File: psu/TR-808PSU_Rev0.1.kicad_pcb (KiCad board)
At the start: 2 copper layers, 142.9 x 119.4 mm, 67 parts, among them IC1 uA7805, IC2 TA7179P, P1 1, P10 10, P11 11, P12 12, P13 13, P14 14, P15 15, P16 16, P17 17, P18 18, P19 19, P2 2, P20 20, P21 21, P22 22, P3 3, P4 4, P5 5, P6 6, P7 7, P8 8, P9 9, Q1 2SB596, Q2 2SD880

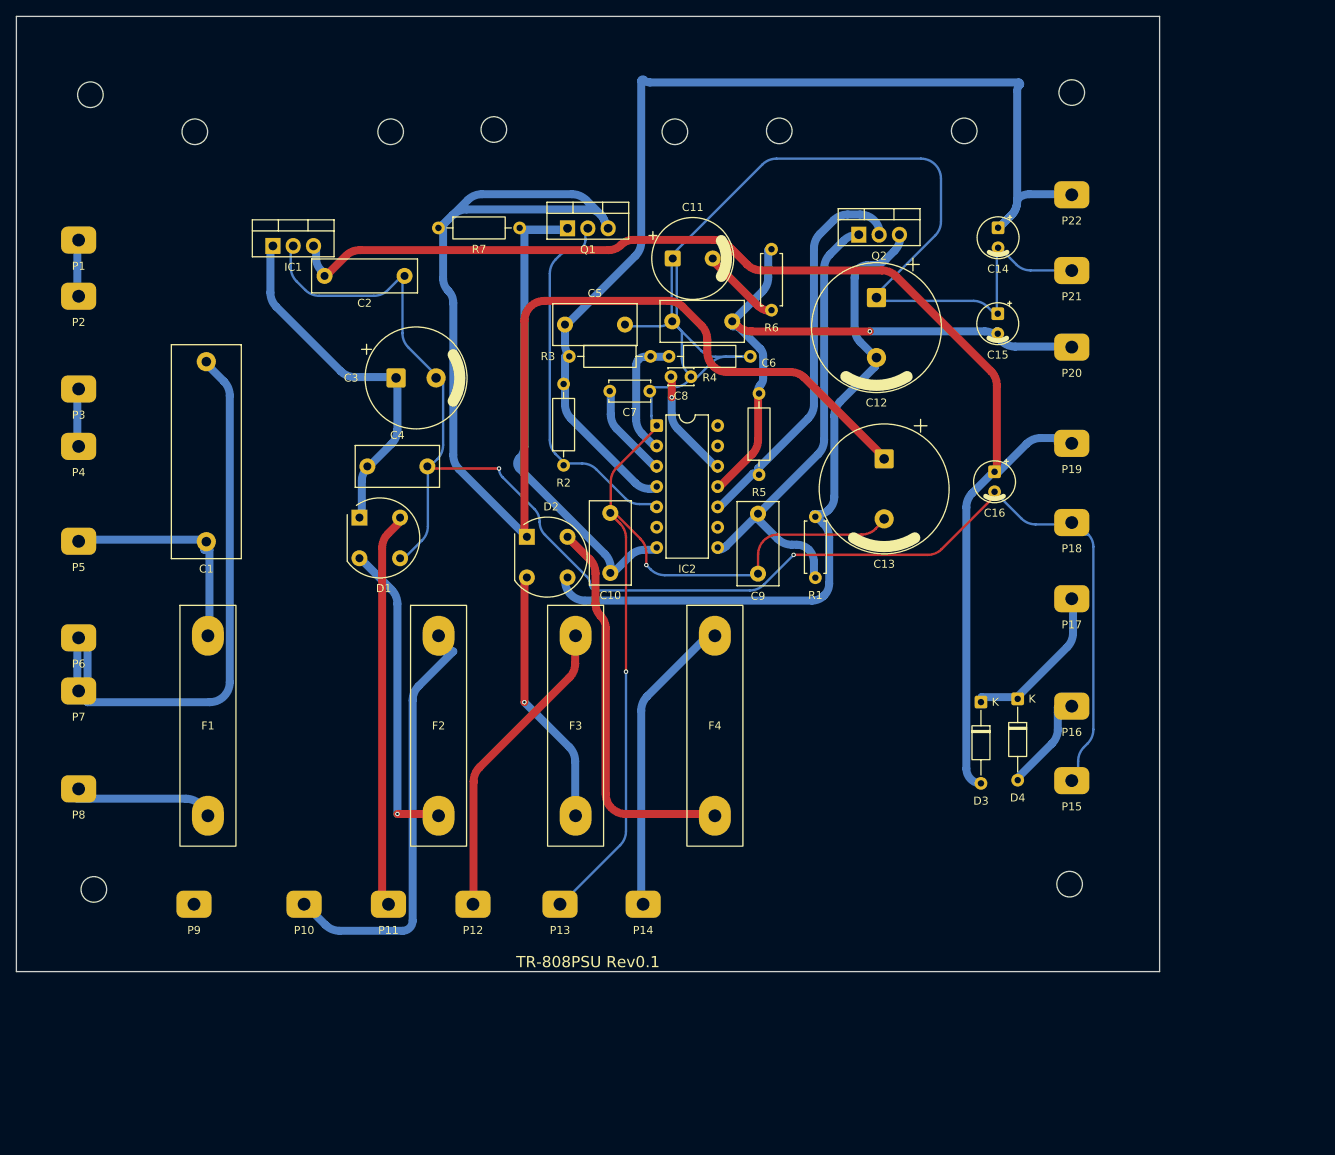
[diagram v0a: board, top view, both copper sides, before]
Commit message: Alle Bahnen 1,0 mm, Pad-Haarnadeln entfernt, Beschriftung frei von Bahnen
verbreitern.py (schmale Netze auf 1,0 mm, DRC-geprueft), padstummel.py (Knicke im Pad),
silk.py meidet Bahnen. DRC 0 Fehler, 0 offen, Netzabstand 6,5 mm.

Co-Authored-By: Claude Sonnet 5.5 <noreply@anthropic.com>
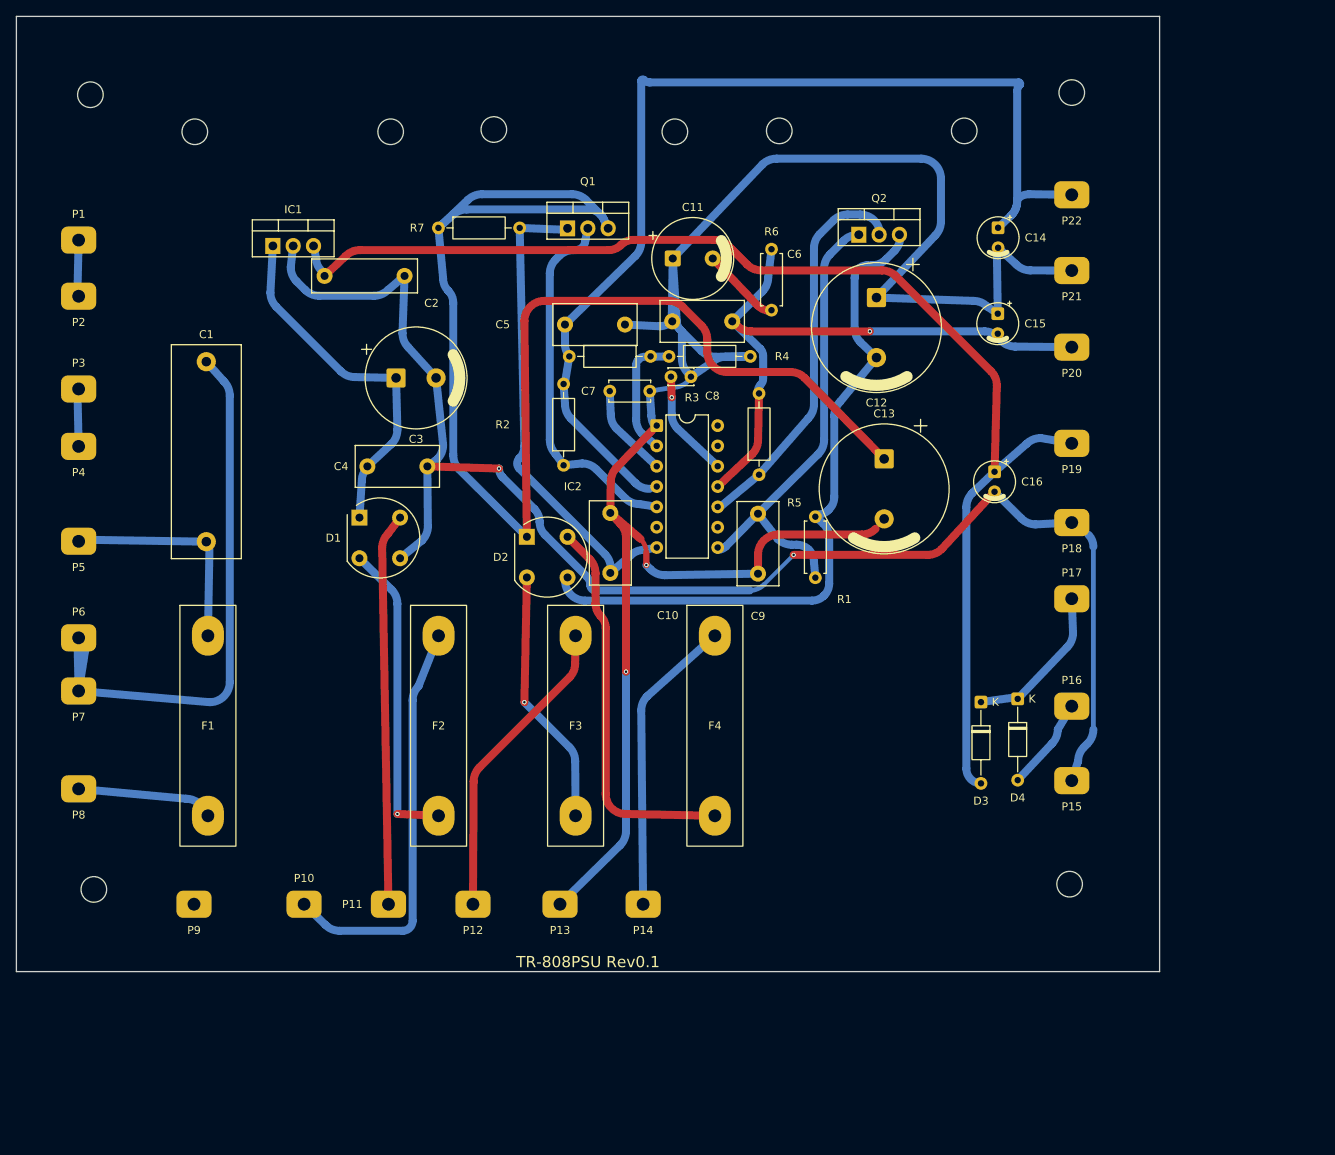
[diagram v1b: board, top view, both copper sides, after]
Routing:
- net /GND15: track 269.0 -> 256.8 mm
- net /GND5: track 193.3 -> 185.4 mm
- net /VB1: track 67.6 -> 59.9 mm
- net /+15V: track 142.3 -> 135.4 mm
- net /-15V: track 82.9 -> 76.7 mm
- net /+5V: track 165.8 -> 159.8 mm
- net /RAW15N: track 89.9 -> 86.3 mm
- net /PRI_8: track 18.9 -> 15.4 mm
- net /AC5_RAW: track 55.0 -> 51.8 mm
- net /SW_A: track 29.7 -> 26.9 mm
- net /SW_B: track 77.8 -> 75.2 mm
- net /RAW5: track 47.6 -> 45.1 mm
- net /RAW15P: track 174.9 -> 173.1 mm
- net /BAT_P: track 13.2 -> 11.6 mm
- net /ADJ: track 16.5 -> 15.0 mm
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
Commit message: Mehr Abstand: Regel 0,25 mm, Bahnen neu, Nachbessern der Breite
Abstandsregel von 0,2 auf 0,25 mm (Router, Glaetten, DRC); verbreitern.py bessert Reststellen nach,
padstummel.py bindet Boegen in der Padrandzone an, silk.py weicht Bahnen aus.

Co-Authored-By: Claude Sonnet 5.5 <noreply@anthropic.com>
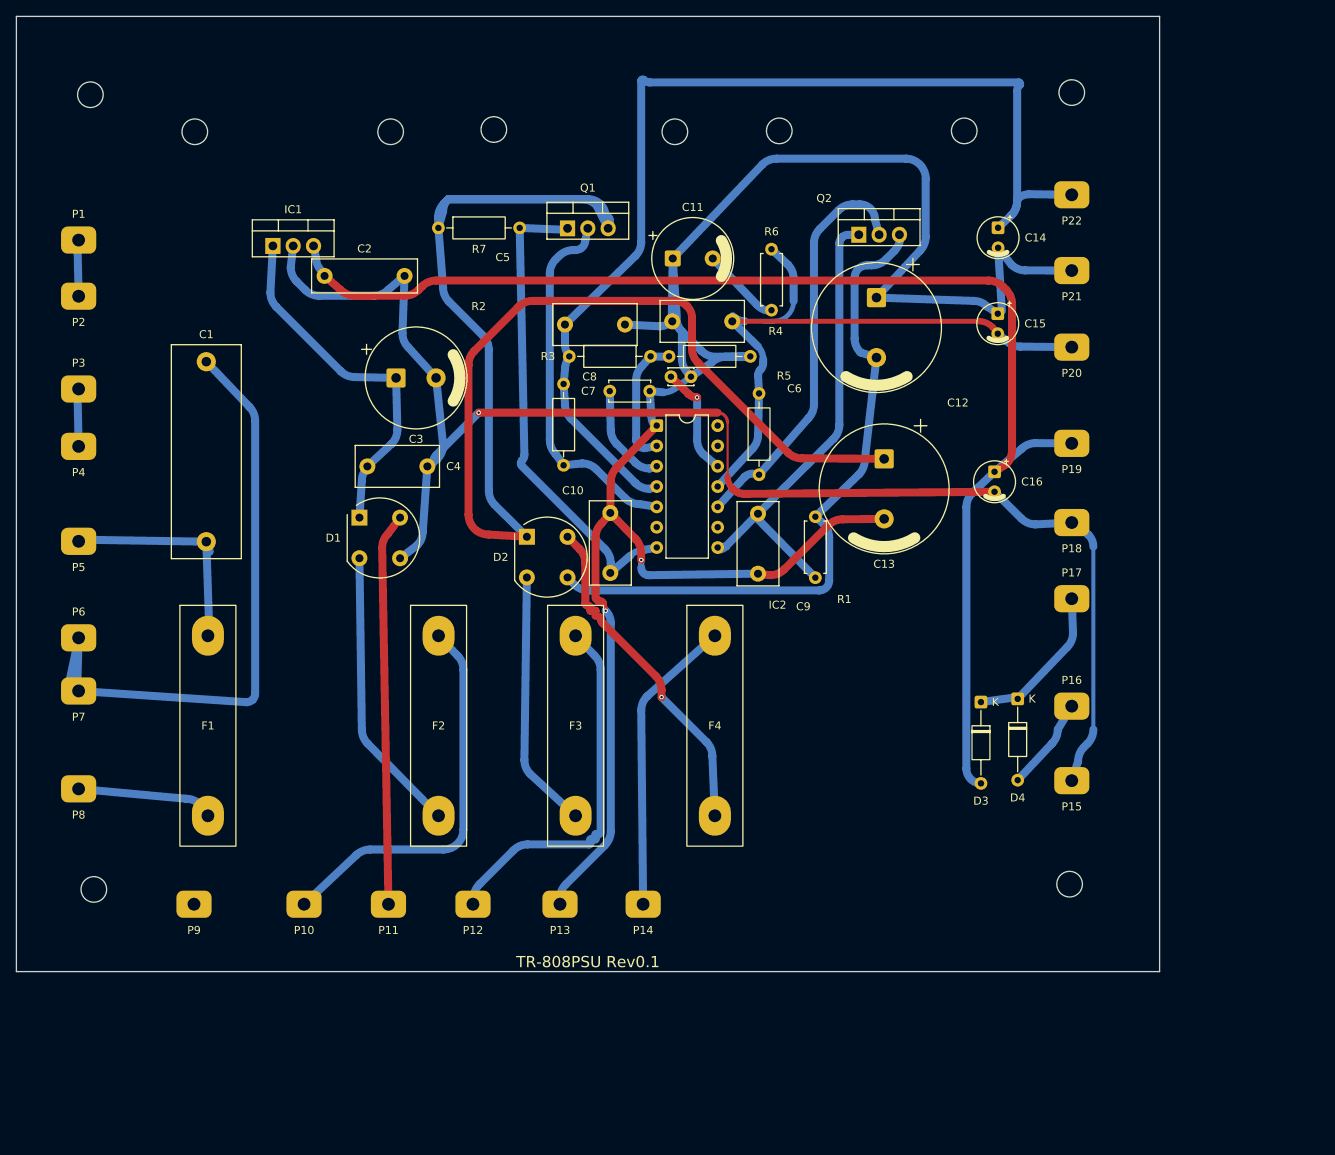
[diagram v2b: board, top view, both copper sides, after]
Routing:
- net /RAW15P: track 173.1 -> 191.3 mm
- net /-15V: track 76.7 -> 84.4 mm, vias 1 -> 0
- net /AC15_RAW_A: track 38.6 -> 46.0 mm
- net /+5V: track 159.8 -> 166.3 mm
- net /AC15_B: track 48.8 -> 42.8 mm, vias 0 -> 1
- net /SW_A: track 26.9 -> 30.9 mm
- net /SW_B: track 75.2 -> 79.0 mm
- net Net-(D1-Pad2): track 39.0 -> 36.0 mm, vias 1 -> 0
- net /AC5_RAW: track 51.8 -> 49.2 mm
- net /GND15: track 256.8 -> 254.4 mm
- net /COL2: track 49.2 -> 50.6 mm
- net /RAW15N: track 86.3 -> 85.0 mm
- net /COMP1: track 11.7 -> 13.0 mm
- net /+15V: track 135.4 -> 136.6 mm
- net /ADJ: track 15.0 -> 16.2 mm
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
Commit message: Zickzack-Stuecke in den Bahnen gerade gezogen (zickzack.py)
Folgen aus kurzen Teilen werden durch ein Segment ersetzt, wenn die DRC danach keinen
neuen Fehler zeigt (9 von 10 Stellen). Beispiel: Treppe unter F3.

Co-Authored-By: Claude Sonnet 5.5 <noreply@anthropic.com>
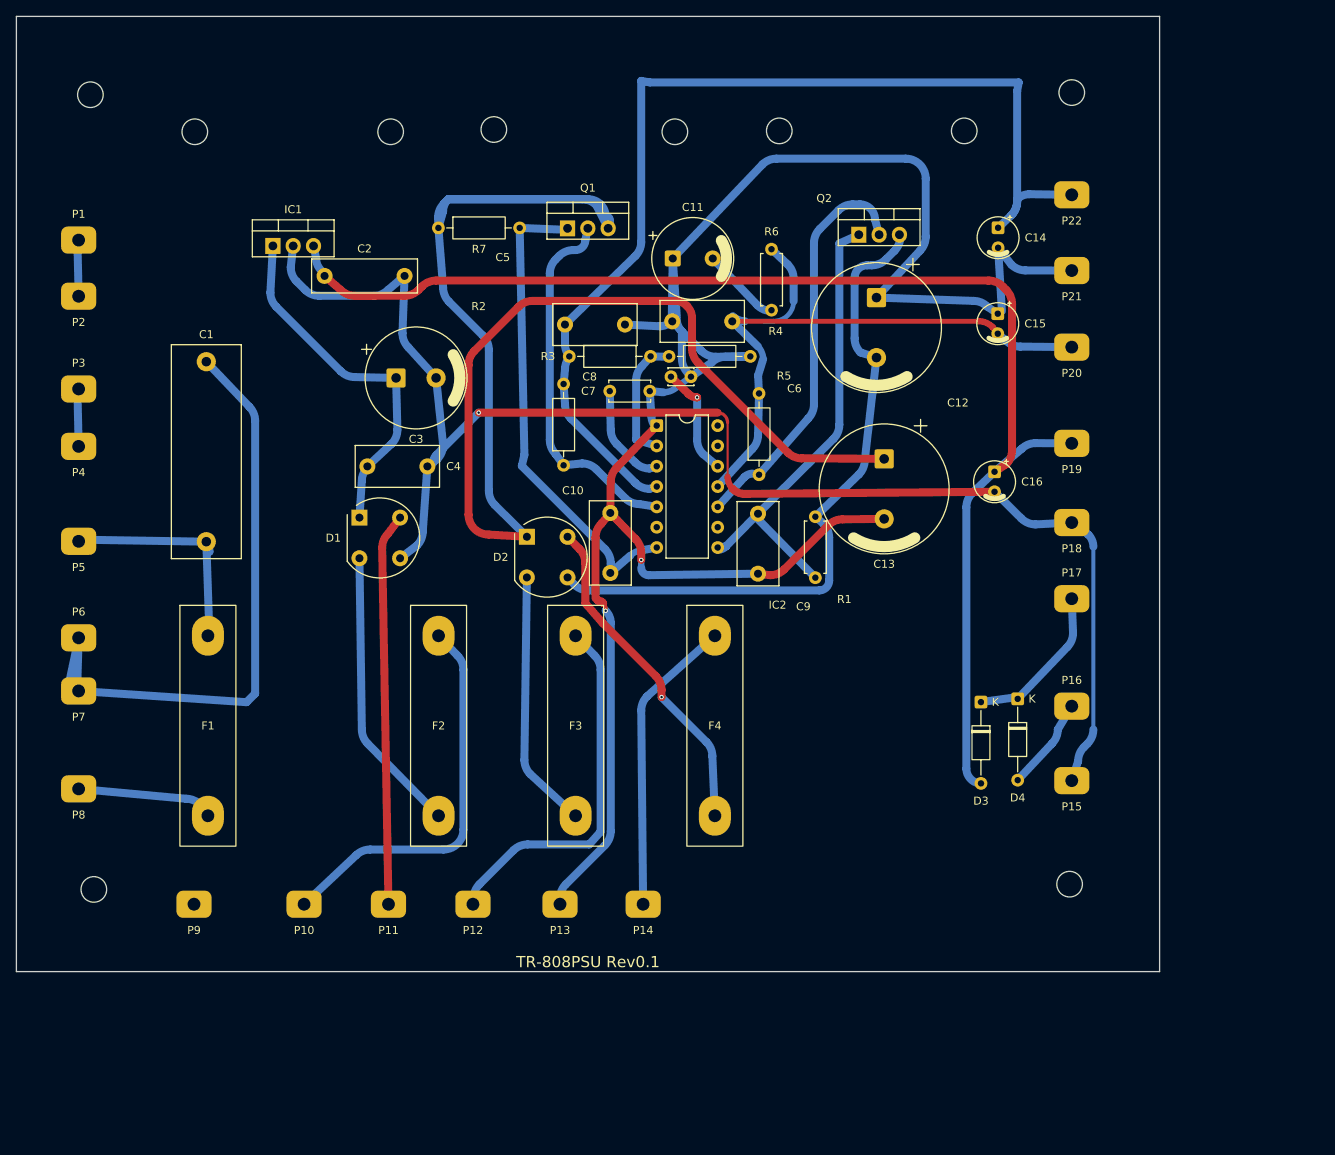
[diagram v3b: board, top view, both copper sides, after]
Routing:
- net /AC15_B: track 42.8 -> 41.9 mm
- net /AC15_RAW_A: track 46.0 -> 45.4 mm
- net /ADJ: track 16.2 -> 15.7 mm

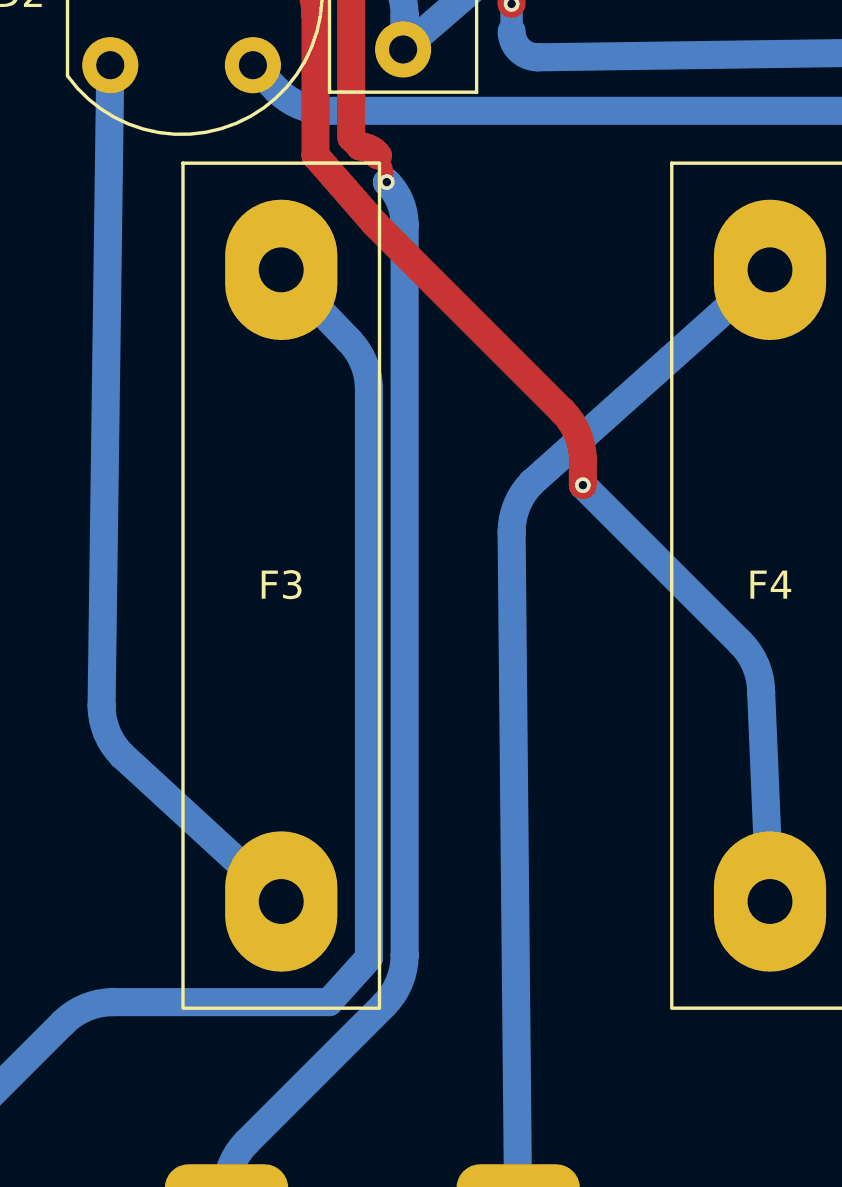
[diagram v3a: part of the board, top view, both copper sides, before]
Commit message: GND15 neben F3 verlegt: 2,2 mm Abstand statt 0,27 mm
korrekturen.py (DRC-geprueft, in make.py eingehaengt).

Co-Authored-By: Claude Sonnet 5.5 <noreply@anthropic.com>
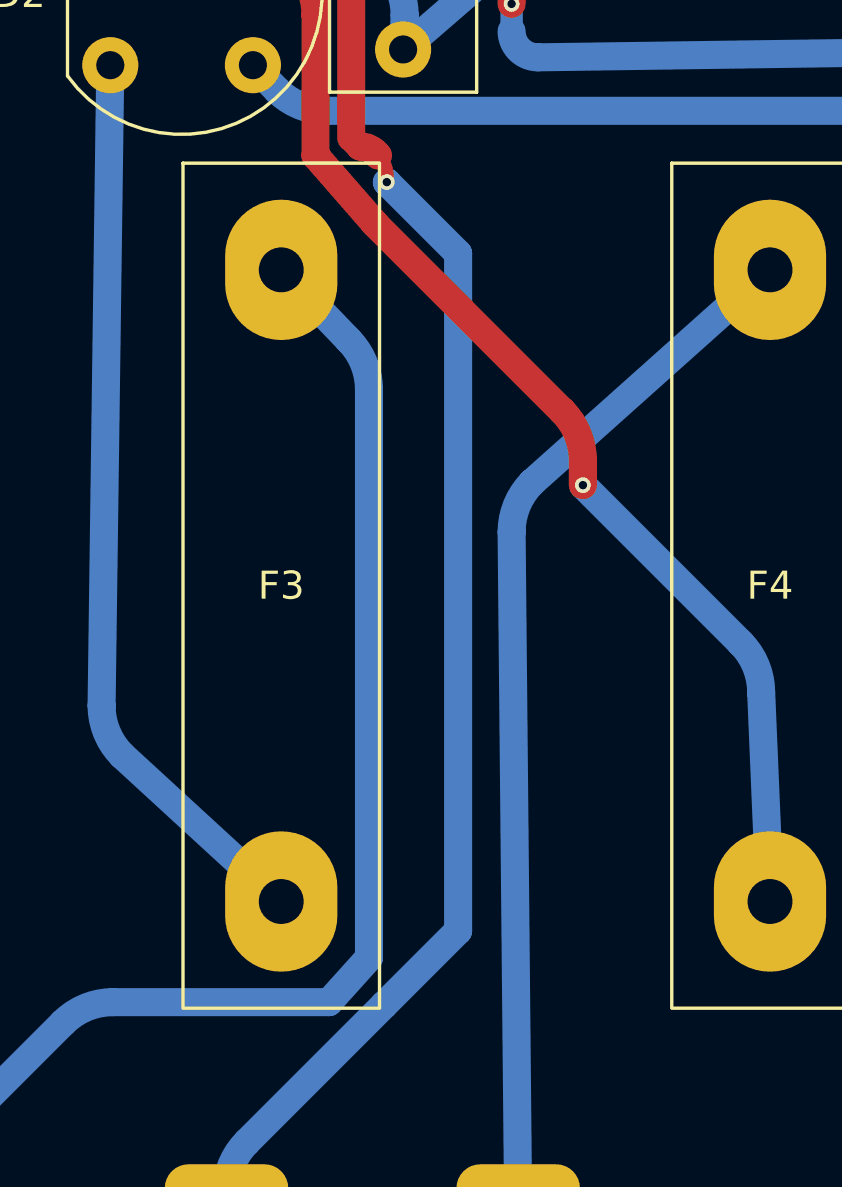
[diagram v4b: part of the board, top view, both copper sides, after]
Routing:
- net /GND15: track 254.4 -> 256.2 mm
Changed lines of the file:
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@@
-	)
-	(segment
-		(start 74.295 75.8101)
-		(end 74.295 101.8345)
-		(width 1)
-		(layer "B.Cu")
-		(net "/GND15")
 	)
 	(segment
@@
 		(mid 78.3784 69.5766)
 		(end 79.0385 69.85)
-		(width 1)
-		(layer "B.Cu")
-		(net "/GND15")
-	)
-	(arc
-		(start 73.6727 74.3077)
-		(mid 74.1333 74.997)
-		(end 74.295 75.8101)
 		(width 1)
 		(layer "B.Cu")
@@
 		(mid 94.0588 17.9703)
 		(end 93.2478 18.5122)
-		(width 1)
-		(layer "B.Cu")
-		(net "/GND15")
-	)
-	(arc
-		(start 74.295 101.8345)
-		(mid 74.1047 102.7912)
-		(end 73.5628 103.6022)
 		(width 1)
 		(layer "B.Cu")
@@
 		(net "/AC15_B")
 	)
+	(segment
+		(start 73.6727 74.3077)
+		(end 76.2000 76.8350)
+		(width 1)
+		(layer "B.Cu")
+		(net "/GND15")
+	)
+	(segment
+		(start 76.2000 76.8350)
+		(end 76.2000 100.9650)
+		(width 1)
+		(layer "B.Cu")
+		(net "/GND15")
+	)
+	(segment
+		(start 76.2000 100.9650)
+		(end 73.5628 103.6022)
+		(width 1)
+		(layer "B.Cu")
+		(net "/GND15")
+	)
 )

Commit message: Handanpassung uebernommen, C8 und loses Bahnende korrigiert
Von Hand: Q2/R7/D3/C8 leicht verschoben, Bahnen teils neu. Korrigiert (korrekturen.py, DRC-geprueft):
C8-Abstaende, GND15-Ende bei (113/21), Polaritaetsbalken der kleinen Elkos nicht mehr auf dem Pad.
Fertigungsdaten, Ausdruck, Plots neu. DRC 0 Fehler, 0 offen.

Co-Authored-By: Claude Sonnet 5.5 <noreply@anthropic.com>
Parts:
- moved Q2 0.80 mm to (105.3, 26.5)
- moved D3 0.37 mm to (120.5, 85.3)
- moved C8 0.30 mm to (81.8, 45.3)
- moved R7 0.21 mm to (52.7, 26.6)
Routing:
- net /GND15: track 256.2 -> 240.5 mm
- net /SW_B: track 78.8 -> 68.7 mm
- net /+15V: track 136.3 -> 131.8 mm
- net /-15V: track 84.3 -> 87.3 mm
- net /GND5: track 185.6 -> 188.5 mm
- net /+5V: track 166.3 -> 168.1 mm
- net /COMP2: track 13.9 -> 15.2 mm
- net /COL2: track 50.6 -> 50.0 mm

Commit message: Kuehlkoerperbohrungen: 21,3 mm Abstand, mittig zu IC1, Q1, Q2
Je Regler ein Paar symmetrisch zum mittleren Anschluss (vorher 22,6 bis 24,5 mm, nicht mittig).
original_placement.py berechnet die Lage jetzt aus den Reglerpositionen. DRC 0 Fehler.

Co-Authored-By: Claude Sonnet 5.5 <noreply@anthropic.com>
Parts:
- moved H9 29.7 mm to (117.0, 34.6)
- moved H5 29.5 mm to (43.8, 34.6)
- moved H7 29.3 mm to (80.6, 34.6)
- moved C10 28.6 mm to (94.1, 90.2)
- moved C9 28.6 mm to (112.5, 90.3)
- moved H4 28.6 mm to (151.5, 129.1)
- moved C1 28.6 mm to (43.6, 86.3)
- moved C14 28.6 mm to (142.6, 47.1)
- moved C16 28.6 mm to (142.1, 77.6)
- moved D3 28.6 mm to (140.4, 106.0)
- moved H3 28.6 mm to (29.5, 129.8)
- moved P7 28.6 mm to (27.6, 105.0)
- moved C13 28.6 mm to (128.3, 76.0)
- moved C2 28.6 mm to (58.4, 53.1)
- moved C4 28.6 mm to (63.7, 76.9)
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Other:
- board text added: "TR-808PSU Rev0.1 by DSL-man.de aka DIYSYNTH.de"
- board text removed: "TR-808PSU Rev0.1"
